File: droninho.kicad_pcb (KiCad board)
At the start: 2 copper layers, 26 x 49 mm, 19 parts, among them J1 M1, J2 M1, J3 M1, J4 M1, J5 Conn_01x02_Pin, Q1 SI2300, Q2 SI2300, Q3 SI2300, Q4 SI2300, U1 ESP32 Dev Kit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

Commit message: Electrical part finished
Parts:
- moved J1 34.2 mm to (110.0, 66.5)
- moved D1 31.7 mm to (115.0, 71.3)
- moved R1 30.1 mm to (117.5, 71.2), turned to 90 degrees
- moved J2 27.8 mm to (157.5, 66.0), turned to -90 degrees
- moved Q1 22.8 mm to (116.1, 66.5), turned to 180 degrees
- moved J5 0.98 mm to (135.5, 135.0)
- moved U2 0.71 mm to (146.8, 111.5)
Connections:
- J5 pad 2: unconnected-(J5-Pin_2-Pad2) -> GND
- U1 pad 1: unconnected-(U1-VIN-Pad1) -> +3.3V

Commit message: Readme added
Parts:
- moved R2 30.7 mm to (148.5, 64.3), turned to -90 degrees
- moved Q3 30.5 mm to (151.9, 109.5)
- moved U2 29.3 mm to (120.8, 125.0), turned to 90 degrees
- moved D4 25.6 mm to (113.7, 113.0)
- moved J4 25.1 mm to (116.0, 118.0), turned to -90 degrees
- moved Q2 23.9 mm to (150.9, 65.0)
- moved D2 22.9 mm to (152.0, 68.5), turned to 180 degrees
- moved R4 20.9 mm to (116.8, 113.0)
- moved R3 19.6 mm to (149.8, 114.0)
- moved D3 18.4 mm to (152.8, 114.0)
- moved J3 16.2 mm to (152.0, 118.5), turned to -90 degrees
- moved Q4 12.7 mm to (115.1, 109.5), turned to 180 degrees
- moved J2 9.60 mm to (151.5, 73.5)
- moved J1 9.22 mm to (116.0, 73.5)
- moved R1 6.88 mm to (118.5, 64.3)
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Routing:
- net PWM4: track 0.00 -> 92.5 mm
- net GND: track 0.00 -> 82.9 mm
- net SDA: track 0.00 -> 65.7 mm
- net SCL: track 0.00 -> 62.4 mm
- net PWM1: track 0.00 -> 39.2 mm
- net +3.3V: track 0.00 -> 37.2 mm
- net PWM3: track 0.00 -> 30.1 mm
- net PWM2: track 0.00 -> 28.1 mm
- net Net-(D1-A): track 0.00 -> 9.31 mm
- net Net-(D2-A): track 0.00 -> 8.71 mm

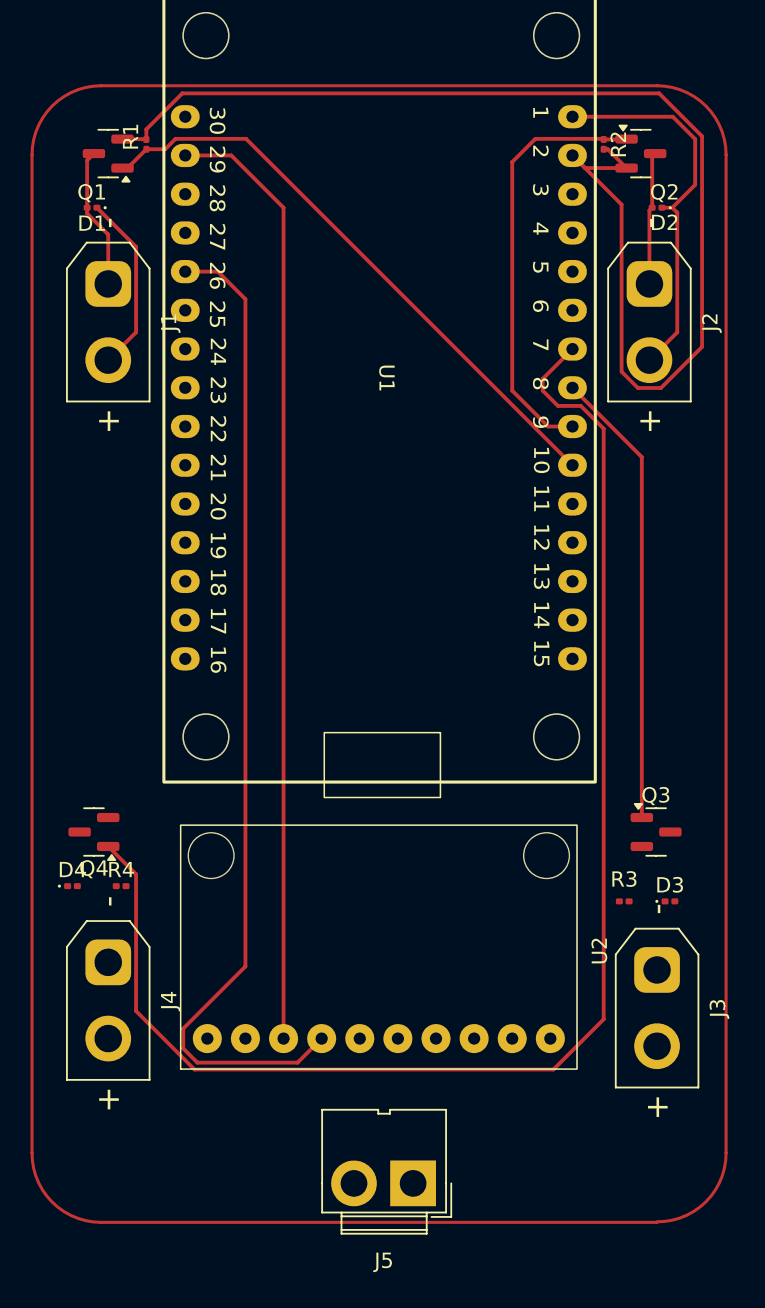
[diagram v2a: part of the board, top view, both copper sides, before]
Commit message: add nets to schematic
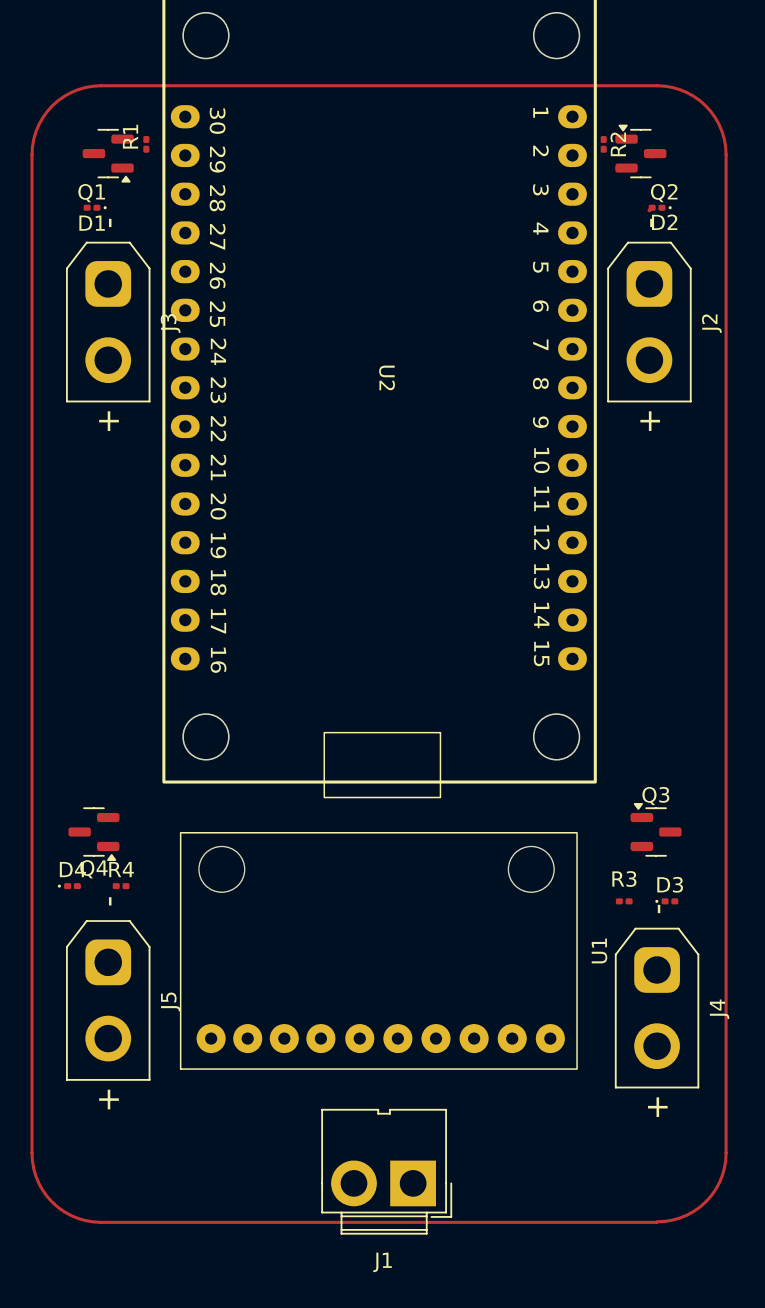
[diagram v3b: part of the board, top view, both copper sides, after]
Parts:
- J2: value M1 -> M2
- J4: renamed from J3; value M1 -> M3
- J5: renamed from J4; value M1 -> M4
- renumbered J5 to J1, J1 to J3, U2 to U1, U1 to U2
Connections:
- net Net-(D1-A) renamed /M1-
- net Net-(D2-A) renamed /M2-
- net Net-(D3-A) renamed /M3-
- net Net-(D4-A) renamed /M4-
- net PWM1 renamed /PWM1
- net PWM2 renamed /PWM2
- net PWM3 renamed /PWM3
- net PWM4 renamed /PWM4
- net SCL renamed /SCL
- net SDA renamed /SDA
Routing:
- net /PWM4: track 92.5 -> 0.00 mm
- net GND: track 82.9 -> 0.00 mm
- net /SDA: track 65.7 -> 0.00 mm
- net /SCL: track 62.4 -> 0.00 mm
- net /PWM1: track 39.2 -> 0.00 mm
- net +3.3V: track 37.2 -> 0.00 mm
- net /PWM3: track 30.1 -> 0.00 mm
- net /PWM2: track 28.1 -> 0.00 mm
- net /M1-: track 9.31 -> 0.00 mm
- net /M2-: track 8.71 -> 0.53 mm

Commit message: ERC OK!
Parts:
- U1: footprint MPU-9250-6500:MPU-9250-6500 -> Library:MPU-9250-6500
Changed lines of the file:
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@@
 	(net 38 "unconnected-(U2-3.3v-Pad16)")
 	(net 39 "unconnected-(U2-GPIO19-Pad25)")
-	(footprint "MPU-9250-6500:MPU-9250-6500"
+	(footprint "Library:MPU-9250-6500"
 		(layer "F.Cu")
 		(at 120.75 125 90)
@@
 			(net 5 "GND")
 			(pinfunction "GND")
-			(pintype "bidirectional")
+			(pintype "power_in")
 			(clearance 0.5)
 		)
@@
 			(net 7 "+3.3V")
 			(pinfunction "VIN")
-			(pintype "power_out")
+			(pintype "power_in")
 		)
 		(pad "2" thru_hole oval
@@
 			(net 5 "GND")
 			(pinfunction "GND")
-			(pintype "bidirectional")
+			(pintype "power_in")
 		)
 		(pad "3" thru_hole oval

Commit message: ERC Done
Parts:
- removed U2: ESP32 Dev Kit, esp32_30_38pin:ESP32_30pin
- added U3: MPU9250/6500, Library:MPU-9250-6500, F.Cu at (121.2, 123.2)
- U1: value MPU9250/6500 -> ESP32 Dev Kit; footprint Library:MPU-9250-6500 -> Library:ESP32_30pin
- moved U1 46.0 mm to (134.1, 81.0)
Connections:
- U1 pad 10: unconnected-(U1-FSYNC-Pad10) -> /PWM1
- U1 pad 3: /SCL -> unconnected-(U1-GPIO13-Pad3)
- U1 pad 4: /SDA -> unconnected-(U1-GPIO12-Pad4)
- U1 pad 7: unconnected-(U1-AD0-Pad7) -> /PWM4
- U1 pad 8: unconnected-(U1-INT-Pad8) -> /PWM3
- U1 pad 9: unconnected-(U1-NCS-Pad9) -> /PWM2

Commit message: PCB feito.
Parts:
- moved R2 29.4 mm to (160.9, 91.0)
- moved Q2 29.2 mm to (163.9, 91.0)
- moved R1 28.4 mm to (129.4, 90.6)
- moved Q1 27.6 mm to (126.4, 90.5)
- moved D2 23.7 mm to (165.5, 88.0), turned to 0 degrees
- moved D1 21.7 mm to (125.3, 87.5), turned to 0 degrees
- moved U3 13.7 mm to (132.3, 131.2)
- moved J2 13.0 mm to (163.5, 78.5)
- moved R4 12.9 mm to (129.7, 114.7), turned to 90 degrees
- moved U1 12.5 mm to (145.4, 86.2), turned to -90 degrees
- moved D4 12.5 mm to (124.8, 118.5)
- moved J5 12.4 mm to (127.0, 123.7)
- moved J4 12.2 mm to (163.0, 123.7)
- moved Q3 12.2 mm to (162.9, 114.6)
- moved Q4 12.2 mm to (126.1, 114.6)
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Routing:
- net GND: track 0.00 -> 178.1 mm, vias 0 -> 4
- net +3.3V: track 0.00 -> 171.3 mm, vias 0 -> 1
- net /SCL: track 0.00 -> 65.7 mm
- net /SDA: track 0.00 -> 57.1 mm
- net /PWM2: track 0.00 -> 55.5 mm
- net /PWM3: track 0.00 -> 43.1 mm, vias 0 -> 1
- net /PWM4: track 0.00 -> 40.3 mm, vias 0 -> 1
- net /M1-: track 0.00 -> 14.4 mm
- net /M2-: track 0.53 -> 14.6 mm
- net /PWM1: track 0.00 -> 13.4 mm
- net /M4-: track 0.00 -> 9.83 mm
- net /M3-: track 0.00 -> 9.52 mm
- added copper zone on B.Cu, net GND
- added copper zone on F.Cu, net GND
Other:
- board size 26 x 49 mm -> 48 x 76.5 mm

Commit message: Footprints checked.
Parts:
- D1, D2, D3, D4: footprint Diode_SMD:D_0201_0603Metric -> Diode_SMD:D_SOD-110
- J1: footprint Connector:JWT_A3963_1x02_P3.96mm_Vertical -> Connector_JST:JST_EH_B2B-EH-A_1x02_P2.50mm_Vertical
- J2, J3, J4, J5: footprint Connector_AMASS:AMASS_XT30UPB-F_1x02_P5.0mm_Vertical -> Connector_JST:JST_PH_B2B-PH-K_1x02_P2.00mm_Vertical
- R1, R2, R3, R4: footprint Resistor_SMD:R_0201_0603Metric -> Resistor_SMD:R_0805_2012Metric_Pad1.20x1.40mm_HandSolder
- moved Q2 3.73 mm to (165.8, 94.3)
- moved Q3 3.73 mm to (166.1, 112.6)
- moved Q4 3.18 mm to (125.0, 111.7)
- moved R2 3.10 mm to (161.5, 94.0)
- moved R4 2.92 mm to (129.6, 111.8)
- moved J2 2.84 mm to (164.7, 81.1)
- moved R3 2.77 mm to (161.5, 112.8)
- moved Q1 2.61 mm to (124.4, 92.2)
- moved J3 2.42 mm to (126.7, 80.9)
- moved D3 2.08 mm to (164.8, 117.3)
- moved D2 1.95 mm to (165.9, 89.9)
- moved R1 1.56 mm to (128.9, 92.0)
- moved J4 1.35 mm to (164.2, 124.2)
- moved D1 1.34 mm to (126.5, 88.2)
- moved J1 1.20 mm to (144.3, 135.3)
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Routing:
- net GND: track 178.1 -> 35.1 mm, vias 4 -> 1
- net /PWM2: track 55.5 -> 36.2 mm, vias 0 -> 1
- net +3.3V: track 171.3 -> 184.7 mm, vias 1 -> 0
- net /PWM4: track 40.3 -> 28.8 mm, vias 1 -> 0
- net /M4-: track 9.83 -> 20.7 mm
- net /PWM1: track 13.4 -> 22.4 mm, vias 0 -> 1
- net /M3-: track 9.52 -> 12.7 mm
- net /PWM3: track 43.1 -> 44.6 mm
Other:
- board size 48 x 76.5 mm -> 48 x 81.6 mm

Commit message: PCB finalizado.
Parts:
- removed U1: ESP32 Dev Kit, Library:ESP32_30pin
- added J6: I2C, Connector:FanPinHeader_1x04_P2.54mm_Vertical, F.Cu at (126.2, 97.9)
- added J7: TXD0/RXD0, Connector:FanPinHeader_1x04_P2.54mm_Vertical, F.Cu at (163.8, 99.4)
- added J8: I2C, Connector:FanPinHeader_1x04_P2.54mm_Vertical, F.Cu at (163.8, 112.3)
- added U2: ESP32 Dev Kit, Library:ESP32_30pin, F.Cu at (145.3, 86.0)
- moved D2 10.1 mm to (164.0, 80.0)
- moved R2 9.68 mm to (161.7, 84.3)
- moved Q2 9.68 mm to (165.9, 84.6)
- moved D1 9.08 mm to (126.0, 79.2), turned to 180 degrees
- moved J2 8.94 mm to (164.2, 72.2)
- moved J3 8.73 mm to (126.9, 72.2)
- moved R1 8.37 mm to (128.5, 83.7)
- moved Q1 8.37 mm to (124.1, 83.8)
- moved R4 6.54 mm to (129.8, 118.3)
- moved Q4 6.54 mm to (125.1, 118.2)
- moved Q3 5.31 mm to (165.8, 117.9)
- moved D3 5.31 mm to (164.4, 122.6)
- moved R3 5.31 mm to (161.2, 118.1)
- moved D4 5.18 mm to (125.2, 122.7)
- moved U3 4.93 mm to (132.1, 136.1)
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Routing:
- net GND: track 35.1 -> 128.7 mm, vias 1 -> 3
- net /SDA: track 57.1 -> 89.3 mm
- net /TXD0: track 0.00 -> 30.4 mm
- net +3.3V: track 184.7 -> 215.0 mm
- net /SCL: track 65.7 -> 94.7 mm, vias 0 -> 1
- net /TXD2: track 0.00 -> 28.7 mm
- net /RXD0: track 0.00 -> 24.4 mm
- net /RXD2: track 0.00 -> 24.3 mm
- net /PWM1: track 22.4 -> 8.84 mm, vias 1 -> 0
- net /PWM4: track 28.8 -> 41.5 mm, vias 0 -> 1
- net /M4-: track 20.7 -> 10.2 mm
- net /PWM3: track 44.6 -> 50.7 mm
- net /M3-: track 12.7 -> 10.4 mm
- net /M1-: track 14.2 -> 15.7 mm
- net /PWM2: track 36.2 -> 35.5 mm
- added copper zone on F.Cu, net (none)
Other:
- outline, holes or cut-outs redrawn
